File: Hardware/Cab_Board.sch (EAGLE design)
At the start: 154 parts, among them J6 3PCV-03-006, SW1 MF-SW-TACT-4.2MM, SW2 MF-SW-TACT-4.2MM, SW3 MF-SW-TACT-4.2MM, U1 P8X32A-Q44, U10 MAX31855KASA+, U11 MAX31855KASA+, U12 G3VM-61GR2(TR05), U13 G3VM-61GR2(TR05), U14 CD74HC595M96, U15 G3VM-61GR2(TR05), U16 CD74HC165M96, U17 G3VM-61GR2(TR05), U18 G3VM-61GR2(TR05), U19 G3VM-61GR2(TR05), U2 G3VM-61GR2(TR05), U20 G3VM-61GR2(TR05), U21 G3VM-61GR2(TR05), U22 G3VM-61GR2(TR05), U23 G3VM-61GR2(TR05), U24 G3VM-61GR2(TR05), U25 G3VM-61GR2(TR05), U26 G3VM-61GR2(TR05), U27 FXOS8700CQR1, U28 ACPL-C870-000E, U29 MAX11613EUA+, U3 G3VM-61GR2(TR05), U30 TPS7B6933QDCYRQ1, U4 MAX31855KASA+, U5 LM22678TJ-5.0/NOPB, U6 ADP3338AKCZ-3.3-RL, U7 CAT24C512WI-GT3, U8 G3VM-61GR2(TR05), U9 MAX31855KASA+, X1 ABMM-6.000MHZ-B2-T

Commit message: new power input
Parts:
- removed 3.3V, 5V: (no value), PP_Connectors:TEST_POINT_SINGLE_KEYSTONE_5115-5119
- removed 3.3V_PWR: MF-LED-0805-RED, PP_LED:LED_SINGLE_0805
- removed C14: 1uf, PP_Passives:CAPACITOR_NON_POLAR_0805
- removed C15: 1000uF, PP_Passives:CAPACITOR_POLARIZED_10MM_SMD
- removed C16, C23, C32, C33, C34, C35, C38, C39: 0.1uF, PP_Passives:CAPACITOR_NON_POLAR_0805
- removed C17: 10uF, PP_Passives:CAPACITOR_NON_POLAR_1206
- removed C22, C44, C45: 10uF, PP_Passives:CAPACITOR_NON_POLAR_1210
- removed C24: 47uF, PP_Passives:CAPACITOR_POLARIZED_6.3MM_SMD
- removed C27: 0.01uF, PP_Passives:CAPACITOR_NON_POLAR_0805
- removed C28: 180uF, PP_Passives:CAPACITOR_POLARIZED_8MM_SMD
- removed C29, C30: 4.7uF, PP_Passives:CAPACITOR_NON_POLAR_1210
- removed C42: .1uF, PP_Passives:CAPACITOR_NON_POLAR_0603
- removed D10, D7, D8, D9: NUP2105LT1G, PP_Passives:TVS_DIODE_DUALSOT-23
- removed J2, J3, J4, J5: (no value), PP_Connectors:CON_01X02_1546215-2
- removed L3: 6.8uH, PP_Passives:INDUCTOR_IHLP-5050
- removed PROP_TC: TC2030-NL, PP_Connectors:CON_02X03_TC2030
- removed PROP_UART: (no value), PP_Connectors:CON_01X06_2.54MM_PIN_HEADER
- removed R11: 330, PP_Passives:RESISTOR_0603
- removed R2: 470K, PP_Passives:RESISTOR_0603
- removed R28, R29, R30, R31, R32, R33, R34, R35, R36, R37, R38, R39, R40, R41, R42, R43, R44, R45: (no value), MF_Passives:RESISTOR_0603
- removed RELAYS, SWITCHS: (no value), PP_Connectors:CON_01X10_1-282834-0
- removed U10, U11, U4, U9: MAX31855KASA+, PP_Sensors:MAX31855
- removed U12, U13, U15, U17, U18, U19, U20, U21, U22, U23, U24, U25, U26, U8: G3VM-61GR2(TR05), PP_DigitalIC:G3VM-61GR2
- removed U14: CD74HC595M96, PP_DigitalIC:CD74HC595M96
- removed U16: CD74HC165M96, PP_DigitalIC:CD74HC165M96
- removed U28: ACPL-C870-000E, PP_AnalogIC:ACPL-C87X
- removed U30: TPS7B6933QDCYRQ1, MF_IC_Power:TPS7B6933QDCYRQ1
- removed U5: LM22678TJ-5.0/NOPB, PP_PowerIC:LM22678
- removed U6: ADP3338AKCZ-3.3-RL, PP_PowerIC:LINEAR_VOTLAGE_REGULATORS_ADP3338
- added C20: 0.1uF, PP_Passives:CAPACITOR_NON_POLAR_0805
- added D1: TPSMB33A, PP_Passives:DIODE_DO-214AA
- added FTDI_CABLE: (no value), PP_Connectors:CON_01X06_2.54MM_PIN_HEADER
- added L1: XPL2010-104MLC, PP_Passives:INDUCTOR_XPL2010
- added TAG_CONNECT: TC2030-NL, PP_Connectors:CON_02X03_TC2030
- C1, C11, C12, C2, C25, C26, C3, C31, C37, C4, C40, C5, C7, C8: MPN (none) -> MF-CAP-0805-0.1uF
- C10: MPN GRJ32DC72A475KE11L -> UMJ325AB7475KMHP
- C13: value 4.7uF -> 470uF; device PP_Passives:CAPACITOR_NON_POLAR_1210 -> PP_Passives:CAPACITOR_POLARIZED_10MM_SMD; MPN GRJ32DC72A475KE11L -> EEH-ZS1V471P
- C36: device PP_Passives:CAPACITOR_NON_POLAR_0805 -> PP_Passives:CAPACITOR_NON_POLAR_1206; MPN (none) -> GRJ32DC72A475KE11L
- C41, C43: value .1uF -> 0.1uF; device PP_Passives:CAPACITOR_NON_POLAR_0603 -> PP_Passives:CAPACITOR_NON_POLAR_0805; MPN (none) -> MF-CAP-0805-0.1uF
- C6: device PP_Passives:CAPACITOR_NON_POLAR_1210 -> PP_Passives:CAPACITOR_NON_POLAR_1206; MPN (none) -> MF-CAP-1206-10uF
- C9: value 0.1uF -> 1uF; MPN (none) -> C0805X105K5RACAUTO
- D3: value VB20100S-E3/8W -> TPSMB18A; device PP_Passives:DIODE_D2PAK(TO-263AB) -> PP_Passives:DIODE_DO-214AA; MPN (none) -> TPSMB18A
- DISP1: MPN (none) -> 61201621621
- J1: value (none) -> 3PCV-04-006; device PP_Connectors:CON_01X02_1546215-2 -> PP_Connectors:CON_01X04_3PCV-04-006; LABEL01 T+ -> ANALOG 0; LABEL02 T- -> ANALOG 1; LABEL03 (none) -> ANALOG 3; LABEL04 (none) -> ANALOG 4; MPN (none) -> 3PCV-04-006
- R10, R17, R9: device PP_Passives:RESISTOR_0805 -> PP_Passives:RESISTOR_0603; MPN (none) -> MF-RES-0603-10K
- R12, R13: MPN (none) -> MF-RES-0603-10K
- R14, R18, R3, R4, R5, R6, R7, R8: value 120 -> 100; MPN (none) -> MF-RES-0603-100
- R15, R16: value 10K -> 15K; device PP_Passives:RESISTOR_0805 -> PP_Passives:RESISTOR_0603; MPN (none) -> MF-RES-0603-15K
- R19, R20: value (none) -> 15K; device MF_Passives:RESISTOR_0603 -> PP_Passives:RESISTOR_0603; MPN (none) -> MF-RES-0603-15K
- R21, R22, R23, R24: value (none) -> 4.7K; device MF_Passives:RESISTOR_0603 -> PP_Passives:RESISTOR_0603; MPN (none) -> MF-RES-0603-4.7K
- R25, R26, R27: value (none) -> 100; device MF_Passives:RESISTOR_0603 -> PP_Passives:RESISTOR_0603; MPN (none) -> MF-RES-0603-100
- SW_D, SW_S, SW_U: value (none) -> 1546215-2; MPN (none) -> 1546215-2
- U2: value G3VM-61GR2(TR05) -> LT8672EMS#PBF; device PP_DigitalIC:G3VM-61GR2 -> PP_PowerIC:LT8672EMS#PBF; MPN (none) -> LT8672EMS#PBF
- U27: MPN (none) -> FXOS8700CQR1
- U29: MPN (none) -> MAX11613EUA+
- U3: value G3VM-61GR2(TR05) -> IPD100N06S403ATMA2; device PP_DigitalIC:G3VM-61GR2 -> PP_DiscreteSemi:MOSFET_N-CHANNEL_SINGLE_TO-252-3; MPN (none) -> IPD100N06S403ATMA2
- U7: MPN (none) -> CAT24C512WI-GT3
- X1: value ABMM-6.000MHZ-B2-T -> 6.0MHz; device MF_Frequency_Control:XTL_7MMX5MM -> MF_Frequency_Control:CYRSTAL_GND_ABMM; MPN (none) -> ABMM-6.000MHZ-B2-T
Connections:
- removed net 12V_BATT_ON: C44.1, U30.VIN
- removed net 5V_PWR: C6.1, DISP1.VCC
- removed net CHASSIS_GND: C44.2, C45.2, R44.P$1, U12.3, U13.3, U15.3, U17.3, U18.3, U19.CATHODE, U2.3, U20.CATHODE, U21.CATHODE, U22.CATHODE, U23.CATHODE, U24.CATHODE, U25.CATHODE, U26.CATHODE, U28.GND1, U28.SHDN, U3.3, U30.GND/ADJ, U8.3
- removed net EXT_5V: C45.1, U28.VDD1, U30.VOUT
- removed net IN_OPTO_1: R29.P$1, U16.D1, U20.4
- removed net IN_OPTO_2: R30.P$1, U16.D2, U21.4
- removed net IN_OPTO_3: R31.P$1, U16.D3, U22.4
- removed net IN_OPTO_4: R32.P$1, U16.D4, U23.4
- removed net IN_OPTO_5: R33.P$1, U16.D5, U24.4
- removed net IN_OPTO_6: R34.P$1, U16.D6, U25.4
- removed net IN_OPTO_7: R35.P$1, U16.D7, U26.4
- removed net N$16: R24.P$2, U15.ANODE
- removed net N$17: R25.P$2, U17.ANODE
- removed net N$18: R26.P$2, U18.ANODE
- removed net N$19: R39.P$1, U23.ANODE
- removed net N$20: R40.P$1, U24.ANODE
- removed net N$21: R41.P$1, U25.ANODE
- removed net N$22: R42.P$1, U26.ANODE
- removed net N$23: R27.P$2, SWITCHS.1
- removed net N$24: R36.P$2, SWITCHS.2
- removed net N$25: R37.P$2, SWITCHS.3
- removed net N$26: R38.P$2, SWITCHS.4
- removed net N$27: R39.P$2, SWITCHS.5
- removed net N$28: R40.P$2, SWITCHS.6
- removed net N$29: R41.P$2, SWITCHS.7
- removed net N$30: R42.P$2, SWITCHS.8
- removed net N$31: R2.2, U5.EN
- removed net N$32: C42.1, R43.P$1, U28.VOUT+
- removed net N$33: R44.P$2, R45.P$2, U28.VIN
- removed net N$36: J5.PIN1, R45.P$1
- removed net N$5: C27.2, D3.CATHODE, L3.P$2, U5.SW
- removed net OUT_0: R19.P$1, U14.Q0
- removed net OUT_1: R20.P$1, U14.Q1
- removed net OUT_2: R21.P$1, U14.Q2
- removed net OUT_3: R22.P$1, U14.Q3
- removed net OUT_4: R23.P$1, U14.Q4
- removed net OUT_5: R24.P$1, U14.Q5
- removed net OUT_6: R25.P$1, U14.Q6
- removed net OUT_7: R26.P$1, U14.Q7
- removed net RLY_0: RELAYS.1, U2.4
- removed net RLY_1: RELAYS.2, U3.4
- removed net RLY_2: RELAYS.3, U8.4
- removed net RLY_3: RELAYS.4, U12.4
- removed net RLY_4: RELAYS.5, U13.4
- removed net RLY_5: RELAYS.6, U15.4
- removed net RLY_6: RELAYS.7, U17.4
- removed net RLY_7: RELAYS.8, U18.4
- removed net SCL_1: R12.1, U1.P10, U27.SCL/SCKL, U29.SCL
- removed net SDA_1: R13.1, U1.P9, U27.SDA/MOSI, U29.SDA
- removed net T+_0: C33.1, D8.1, J1.PIN1, U9.T+
- removed net T+_1: C35.1, D9.1, J2.PIN1, U10.T+
- removed net T+_2: C39.1, D7.1, J3.PIN1, U11.T+
- removed net T+_3: C12.1, D10.1, J4.PIN1, U4.T+
- removed net T-_0: C33.2, D8.2, J1.PIN2, U9.T-
- removed net T-_1: C35.2, D9.2, J2.PIN2, U10.T-
- removed net T-_2: C39.2, D7.2, J3.PIN2, U11.T-
- removed net T-_3: C12.2, D10.2, J4.PIN2, U4.T-
- new net P10: U1.P10
- new net P9: U1.P9
- new net VIN: D1.CATHODE, U2.SOURCE, U3.SOURCE
- net !RES!_PROP: now also FTDI_CABLE.6, TAG_CONNECT.PIN6; no longer PROP_TC.PIN6, PROP_UART.6
- net 12V: no longer C10.1, C14.1, C29.1, C30.1, R2.1, U5.VIN
- net 165_CLK: no longer U16.CLK
- net 165_DATA: no longer U16.QH
- net 165_LOAD: no longer U16.LAT
- net 3.3V: no longer 3.3V.P$1, C11.1, C22.1, C23.1, C24.POS, C32.1, C34.1, C38.1, C7.1, C9.1, R11.1, R15.2, R16.2, R28.P$2, R29.P$2, R30.P$2, R31.P$2, R32.P$2, R33.P$2, R34.P$2, R35.P$2, U10.VCC, U11.VCC, U14.MR, U14.VCC, U16.VCC, U28.VDD2, U4.VCC, U6.OUT, U9.VCC
- net 595_CLK: no longer U14.SHCP
- net 595_DATA: no longer U14.DS
- net 595_LAT: no longer U14.STCP
- net 5V: now also C6.1, DISP1.VCC; no longer 5V.P$1, C13.1, C15.POS, C16.1, C17.1, C28.POS, L3.P$1, U5.FB, U6.IN
- net A0: now also C7.1, R15.1, R24.2; no longer R43.P$2
- net A1: now also C11.1, R16.1, R23.2
- net A2: now also C12.1, R19.1, R22.2
- net A3: now also C20.1, R20.1, R21.2
- net GND: now also C12.2, C13.NEG, C20.2, D3.CATHODE, FTDI_CABLE.1, R21.1, R22.1, R23.1, R24.1, TAG_CONNECT.PIN5, U2.GND; no longer 3.3V_PWR.CATHODE, C13.2, C14.2, C15.NEG, C16.2, C17.2, C22.2, C23.2, C24.NEG, C28.NEG, C29.2, C30.2, C32.2, C34.2, C38.2, C42.2, C9.2, D10.3, D3.ANODE, D7.3, D8.3, D9.3, PROP_TC.PIN5, PROP_UART.1, U10.GND, U11.GND, U12.CATHODE, U13.CATHODE, U14.GND, U14.OE, U15.CATHODE, U16.C_INH, U16.GND, U17.CATHODE, U18.CATHODE, U19.3, U2.CATHODE, U20.3, U21.3, U22.3, U23.3, U24.3, U25.3, U26.3, U28.GND2, U28.VOUT-, U3.CATHODE, U4.GND, U5.GND, U6.GND, U8.CATHODE, U9.GND
- net N$1: now also J1.1, R15.2; no longer R28.P$1, U16.D0, U19.4
- net N$10: now also R25.2, SW_U.PIN1; no longer R38.P$1, U22.ANODE
- net N$11: now also R26.2, SW_S.PIN1; no longer R19.P$2, U2.ANODE
- net N$12: now also R27.2, SW_D.PIN1; no longer R20.P$2, U3.ANODE
- net N$13: now also C10.1, C13.POS, C9.1, L1.P$1, U2.DRAIN, U3.DRAIN; no longer R21.P$2, U8.ANODE
- net N$14: now also C9.2, U2.AUX; no longer R22.P$2, U12.ANODE
- net N$15: now also L1.P$2, U2.AUXSW; no longer R23.P$2, U13.ANODE
- net N$2: now also U2.GATE, U3.GATE; no longer C27.1, U5.BOOT
- net N$3: now also J1.2, R16.2; no longer R27.P$1, U19.ANODE
- net N$4: now also J1.3, R19.2; no longer R36.P$1, U20.ANODE
- net N$6: now also J1.4, R20.2; no longer R37.P$1, U21.ANODE
- net N$9: now also D1.ANODE, D3.ANODE; no longer 3.3V_PWR.ANODE, R11.2
- net RX_PROP: now also FTDI_CABLE.4, TAG_CONNECT.PIN4; no longer PROP_TC.PIN4, PROP_UART.4
- net SCL: now also R12.1, U27.SCL/SCKL, U29.SCL; no longer R15.1
- net SDA: now also R13.1, U27.SDA/MOSI, U29.SDA; no longer R16.1
- net SW_D: now also R27.1; no longer SW_D.PIN1
- net SW_S: now also R26.1; no longer SW_S.PIN1
- net SW_U: now also R25.1; no longer SW_U.PIN1
- net TC_CS_0: no longer U9.!CS
- net TC_CS_1: no longer U10.!CS
- net TC_CS_2: no longer U11.!CS
- net TC_CS_3: no longer U4.!CS
- net TC_SCK: no longer U10.SCK, U11.SCK, U4.SCK, U9.SCK
- net TC_SO: no longer U10.SO, U11.SO, U4.SO, U9.SO
- net TX_PROP: now also FTDI_CABLE.5, TAG_CONNECT.PIN3; no longer PROP_TC.PIN3, PROP_UART.5
- net X0: now also X1.X1; no longer X1.X0
- net X1: now also X1.X0; no longer X1.X1
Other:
- note added: "ANALOG INPUT 12V COMPLIANT"
- note added: "DISPLAY VFD CONNECTOR"
- note added: "EEPROM FOR PROPELLER"
- note added: "IMU AND GYRO"
- note added: "NAV BUTTONS"
- note added: "PROPELLER MCU"
- note added: "PROPELLER PROGRAMMING SETUP"
- note removed: "5V POWER SUPPLY"
- moved on the sheet: 12V, C1, C10, C11, C12, C18, C19, C2, C25, C26, C3, C31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

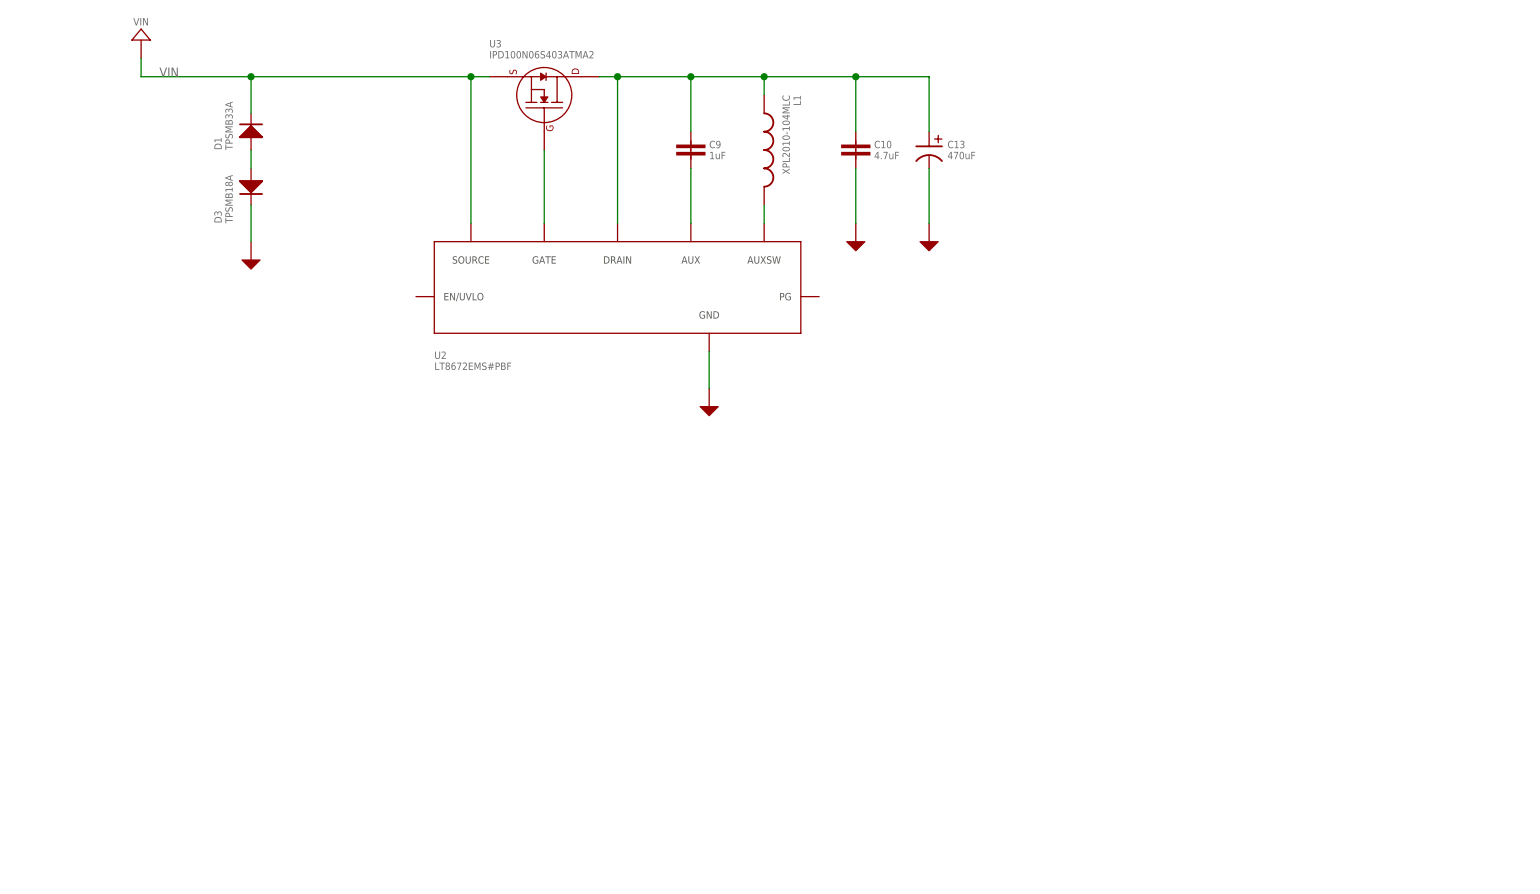
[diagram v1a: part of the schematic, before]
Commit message: added LT8614
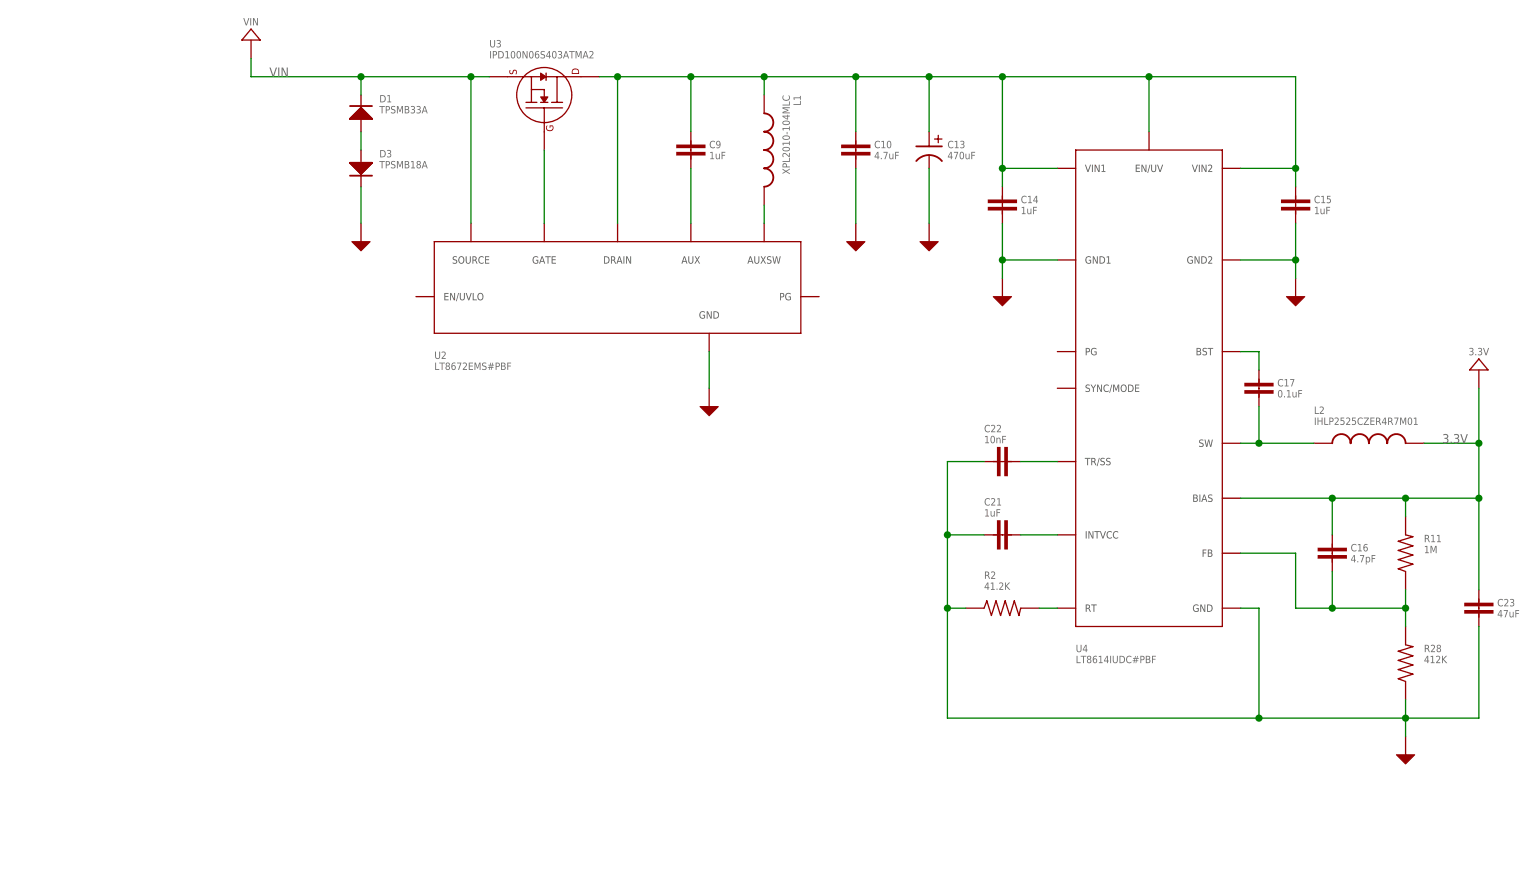
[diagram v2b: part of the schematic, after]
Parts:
- added C14, C15, C21: 1uF, PP_Passives:CAPACITOR_NON_POLAR_0805
- added C16: 4.7pF, PP_Passives:CAPACITOR_NON_POLAR_0603
- added C17: 0.1uF, PP_Passives:CAPACITOR_NON_POLAR_0603
- added C22: 10nF, PP_Passives:CAPACITOR_NON_POLAR_0603
- added C23: 47uF, PP_Passives:CAPACITOR_NON_POLAR_1210
- added L2: IHLP2525CZER4R7M01, PP_Passives:INDUCTOR_IHLP-2525
- added R11: 1M, PP_Passives:RESISTOR_0603
- added R2: 41.2K, PP_Passives:RESISTOR_0603
- added R28: 412K, PP_Passives:RESISTOR_0603
- added U4: LT8614IUDC#PBF, PP_PowerIC:LT8614IUDC#PBF
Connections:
- new net BST: C17.1, U4.BST
- new net FB: C16.2, R11.1, R28.2, U4.FB
- new net INTVCC: C21.2, U4.INTVCC
- new net RT: R2.2, U4.RT
- new net SW: C17.2, L2.P$1, U4.SW
- new net TR/SS: C22.2, U4.TR/SS
- net 3.3V: now also C16.1, C23.1, L2.P$2, R11.2, U4.BIAS
- net GND: now also C14.2, C15.2, C21.1, C22.1, C23.2, R2.1, R28.1, U4.GND, U4.GND1, U4.GND2
- net N$13: now also C14.1, C15.1, U4.EN/UV, U4.VIN1, U4.VIN2
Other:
- moved on the sheet: D1, D3

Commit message: cleaing up schematic more.
8 analog inputs
0-5V Analog in
Thermistors
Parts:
- removed 12V, GND: (no value), PP_Connectors:TEST_POINT_SINGLE_KEYSTONE_5115-5119
- removed C11, C12, C20, C25, C26, C37, C40, C41, C43, C7: 0.1uF, PP_Passives:CAPACITOR_NON_POLAR_0805
- removed C18: 1000uF, PP_Passives:CAPACITOR_POLARIZED_12.5MM_PTH
- removed C19: 220uF, PP_Passives:CAPACITOR_POLARIZED_10MM_SMD
- removed C36: 4.7uF, PP_Passives:CAPACITOR_NON_POLAR_1206
- removed C6: 10uF, PP_Passives:CAPACITOR_NON_POLAR_1206
- removed DISP1: 61201621621, PP_Displays:CU40056-UW1J
- removed J1: 3PCV-04-006, PP_Connectors:CON_01X04_3PCV-04-006
- removed J6: 3PCV-03-006, PP_Connectors:CON_01X03_3PV-03-006
- removed R10, R12, R13, R17, R9: 10K, PP_Passives:RESISTOR_0603
- removed R14, R18, R25, R26, R27, R3, R4, R5, R6, R7, R8: 100, PP_Passives:RESISTOR_0603
- removed R15, R16, R19, R20: 15K, PP_Passives:RESISTOR_0603
- removed R21, R22, R23, R24: 4.7K, PP_Passives:RESISTOR_0603
- removed SW1, SW2, SW3: MF-SW-TACT-4.2MM, MF_Switches:TACT_4.2MM
- removed SW_D, SW_S, SW_U: 1546215-2, PP_Connectors:CON_01X02_1546215-2
- removed TVS1: V18AUMLA2220H, PP_Passives:TVS_DIODE_2220
- removed U27: FXOS8700CQR1, PP_Sensors:FXOS8700CQR1
- removed U29: MAX11613EUA+, PP_AnalogIC:MAX11613EUA+
- added C24, C27, C30: 1uF, PP_Passives:CAPACITOR_NON_POLAR_0805
- added C28: 4.7pF, PP_Passives:CAPACITOR_NON_POLAR_0603
- added C29: 0.1uF, PP_Passives:CAPACITOR_NON_POLAR_0603
- added C32: 10nF, PP_Passives:CAPACITOR_NON_POLAR_0603
- added C33: 47uF, PP_Passives:CAPACITOR_NON_POLAR_1210
- added J2: TBL009-254-02GY-2GY, PP_Connectors:CON_01X02_TBL009-254-02GY-2GY
- added L3: IHLP2525CZER4R7M01, PP_Passives:INDUCTOR_IHLP-2525
- added R29: 41.2K, PP_Passives:RESISTOR_0603
- added R30: 1M, PP_Passives:RESISTOR_0603
- added R31: 243K, PP_Passives:RESISTOR_0603
- added U5: LT8614IUDC#PBF, PP_PowerIC:LT8614IUDC#PBF
- C31: SPICEPREFIX (none) -> C
- D2: value VS-12CWQ10FN-M3 -> BAT54S; device PP_Passives:DIODE_D-PAK(TO-252AA) -> PP_Passives:TVS_DIODE_DUALSOT-23; MPN VS-12CWQ10FN-M3 -> (none)
- U7: SPICEPREFIX (none) -> X
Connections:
- net 165_CLK renamed P13
- net 165_DATA renamed P11
- net 165_LOAD renamed P12
- net 595_CLK renamed P16
- net 595_DATA renamed P14
- net 595_LAT renamed P15
- net TC_CS_0 renamed P22
- net TC_CS_1 renamed P23
- net TC_CS_2 renamed P24
- net TC_CS_3 renamed P25
- net TC_SCK renamed P27
- net TC_SO renamed P26
- removed net 12V: 12V.P$1, C18.POS, C19.POS, D2.CATHODE
- removed net 12V_BATT: D2.ANODE, J6.PIN1, TVS1.P$2
- removed net 5V: C6.1, DISP1.VCC
- removed net A0: C7.1, R15.1, R24.2, U29.A_0
- removed net A1: C11.1, R16.1, R23.2, U29.A_1
- removed net A2: C12.1, R19.1, R22.2, U29.A_2
- removed net A3: C20.1, R20.1, R21.2, U29.A_3
- removed net D4: DISP1.D4, R6.2
- removed net D5: DISP1.D5, R5.2
- removed net D6: DISP1.D6, R4.2
- removed net D7: DISP1.D7, R3.2
- removed net DOME_PWR: J6.PIN3
- removed net E1: DISP1.E1, R8.2
- removed net E2: DISP1.E2, R7.2
- removed net N$1: J1.1, R15.2
- removed net N$10: R25.2, SW_U.PIN1
- removed net N$11: R26.2, SW_S.PIN1
- removed net N$12: R27.2, SW_D.PIN1
- removed net N$3: J1.2, R16.2
- removed net N$4: J1.3, R19.2
- removed net N$6: J1.4, R20.2
- removed net N$7: C26.1, U27.BYP
- removed net N$8: C40.1, U27.CRST
- removed net PROP_D4: R6.1, U1.P3
- removed net PROP_D5: R5.1, U1.P4
- removed net PROP_D6: R4.1, U1.P1
- removed net PROP_D7: R3.1, U1.P2
- removed net PROP_E1: R8.1, U1.P5
- removed net PROP_E2: R7.1, U1.P8
- removed net PROP_R/W: R14.1, U1.P6
- removed net PROP_RS: R18.1, U1.P7
- removed net R/W: DISP1.R/W, R14.2
- removed net RS: DISP1.RS, R18.2
- removed net SW_D: R27.1, R9.2, SW3.P$1, U1.P19
- removed net SW_S: R10.2, R26.1, SW2.P$1, U1.P20
- removed net SW_U: R17.2, R25.1, SW1.P$1, U1.P21
- new net 5.0V: C28.1, C33.1, L3.P$2, R30.2, U5.BIAS
- new net BST1: C29.1, U5.BST
- new net FB1: C28.2, R30.1, R31.2, U5.FB
- new net INTVCC1: C30.2, U5.INTVCC
- new net P1: U1.P1
- new net P19: U1.P19
- new net P2: U1.P2
- new net P20: U1.P20
- new net P21: U1.P21
- new net P3: U1.P3
- new net P4: U1.P4
- new net P5: U1.P5
- new net P6: U1.P6
- new net P7: U1.P7
- new net P8: U1.P8
- new net RT1: R29.2, U5.RT
- new net SW1: C29.2, L3.P$1, U5.SW
- new net TR/SS1: C32.2, U5.TR/SS
- net 3.3V: no longer C25.1, C36.1, C37.1, C41.1, C43.1, R10.1, R12.2, R13.2, R17.1, R9.1, U27.VDD, U27.VDDIO, U29.VCC
- net GND: now also C24.2, C27.2, C30.1, C32.1, C33.2, J2.PIN2, R29.1, R31.1, U5.GND, U5.GND1, U5.GND2; no longer C11.2, C12.2, C18.NEG, C19.NEG, C20.2, C25.2, C26.2, C36.2, C37.2, C40.2, C41.2, C43.2, C6.2, C7.2, DISP1.D0, DISP1.D1, DISP1.D2, DISP1.D3, DISP1.GND, GND.P$1, J6.PIN2, R21.1, R22.1, R23.1, R24.1, SW1.P$4, SW2.P$4, SW3.P$4, SW_D.PIN2, SW_S.PIN2, SW_U.PIN2, TVS1.P$1, U27.GND, U27.RST, U27.SA0/MISO, U27.SA1/CS_B, U29.GND
- net N$13: now also C24.1, C27.1, U5.EN/UV, U5.VIN1, U5.VIN2
- net SCL: no longer R12.1, U27.SCL/SCKL, U29.SCL
- net SDA: no longer R13.1, U27.SDA/MOSI, U29.SDA
- net VIN: now also J2.PIN1
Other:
- note removed: "ANALOG INPUT 12V COMPLIANT"
- note removed: "DISPLAY VFD CONNECTOR"
- note removed: "EEPROM FOR PROPELLER"
- note removed: "IMU AND GYRO"
- note removed: "NAV BUTTONS"
- note removed: "POWER INPUT"
- note removed: "PROPELLER MCU"
- note removed: "PROPELLER PROGRAMMING SETUP"
- moved on the sheet: C1, C2, C3, C31, C4, C5, C8, FTDI_CABLE, R1, TAG_CONNECT, U1, U7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

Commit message: added LTC2986HLX#PBF
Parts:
- added D10, D4, D5, D6, D7, D8, D9: BAT54S, PP_Passives:TVS_DIODE_DUALSOT-23
- added J1: DF11G-16DP-2V(50), PP_Connectors:CON_02X08_DF11G-16DP-2V(50)
- added R10, R3, R4, R5, R6, R7, R8, R9: 330, PP_Passives:RESISTOR_0805
- added U$45: LTC2986HLX#PBF, PP_Sensors:LTC2986HLX#PBF
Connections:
- removed net P0: U1.P0
- removed net P1: U1.P1
- new net ANALOG_MCU_0: D2.3, R3.1
- new net ANALOG_MCU_1: D4.3, R4.1
- new net ANALOG_MCU_2: D5.3, R5.1
- new net ANALOG_MCU_3: D6.3, R6.1
- new net ANALOG_MCU_4: D7.3, R7.1
- new net ANALOG_MCU_5: D8.3, R8.1
- new net ANALOG_MCU_6: D9.3, R9.1
- new net ANALOG_MCU_7: D10.3, R10.1
- new net ANALOG_WORLD_0: R3.2
- new net ANALOG_WORLD_1: R4.2
- new net ANALOG_WORLD_2: R5.2
- new net ANALOG_WORLD_3: R6.2
- new net ANALOG_WORLD_4: R7.2
- new net ANALOG_WORLD_5: R8.2
- new net ANALOG_WORLD_6: R9.2
- new net ANALOG_WORLD_7: R10.2
- new net GPIO0: J1.11
- new net GPIO1: J1.12
- new net GPIO2: J1.9
- new net GPIO3: J1.10
- new net GPIO4: J1.13
- new net LCD_RX: J1.1, U1.P1
- new net LCD_TX: J1.2, U1.P0
- net 5.0V: now also D10.1, D2.1, D4.1, D5.1, D6.1, D7.1, D8.1, D9.1, J1.16
- net GND: now also D10.2, D2.2, D4.2, D5.2, D6.2, D7.2, D8.2, D9.2, J1.15
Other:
- moved on the sheet: D2

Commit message: Control side of LTC2986HLX done.
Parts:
- removed D10, D2, D4, D5, D6, D7, D8, D9: BAT54S, PP_Passives:TVS_DIODE_DUALSOT-23
- removed R10, R6, R7, R8, R9: 330, PP_Passives:RESISTOR_0805
- removed U$45: LTC2986HLX#PBF, PP_Sensors:LTC2986HLX#PBF
- added C11, C12, C18, C19, C35, C36, C6, C7: 0.1uF, PP_Passives:CAPACITOR_NON_POLAR_0805
- added C20: 1uF, PP_Passives:CAPACITOR_NON_POLAR_0805
- added C25, C26, C34: 10uF, PP_Passives:CAPACITOR_NON_POLAR_1210
- added U6: IPD100N06S403ATMA2, PP_DiscreteSemi:MOSFET_N-CHANNEL_SINGLE_TO-252-3
- added U8: TXB0104DR, PP_DigitalIC:TXB0104DR
- R3, R4: value 330 -> 10K; device PP_Passives:RESISTOR_0805 -> PP_Passives:RESISTOR_0603; MPN (none) -> MF-RES-0603-10K
- R5: value 330 -> 18K; device PP_Passives:RESISTOR_0805 -> PP_Passives:RESISTOR_0603
- U2: value LT8672EMS#PBF -> CAT24C512WI-GT3; device PP_PowerIC:LT8672EMS#PBF -> PP_DigitalIC:EEPROM_I2CSOIC-8_W; MPN LT8672EMS#PBF -> CAT24C512WI-GT3; SPICEPREFIX (none) -> X
- U3: value IPD100N06S403ATMA2 -> LT8672EMS#PBF; device PP_DiscreteSemi:MOSFET_N-CHANNEL_SINGLE_TO-252-3 -> PP_PowerIC:LT8672EMS#PBF; MPN IPD100N06S403ATMA2 -> LT8672EMS#PBF
- U7: value CAT24C512WI-GT3 -> LTC2986HLX-1#PBF; device PP_DigitalIC:EEPROM_I2CSOIC-8_W -> PP_Sensors:LTC2986HLX#PBF; MPN CAT24C512WI-GT3 -> LTC2986HLX-1#PBF; SPICEPREFIX X -> (none)
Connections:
- removed net ANALOG_MCU_0: D2.3, R3.1
- removed net ANALOG_MCU_1: D4.3, R4.1
- removed net ANALOG_MCU_2: D5.3, R5.1
- removed net ANALOG_MCU_3: D6.3, R6.1
- removed net ANALOG_MCU_4: D7.3, R7.1
- removed net ANALOG_MCU_5: D8.3, R8.1
- removed net ANALOG_MCU_6: D9.3, R9.1
- removed net ANALOG_MCU_7: D10.3, R10.1
- removed net ANALOG_WORLD_0: R3.2
- removed net ANALOG_WORLD_1: R4.2
- removed net ANALOG_WORLD_2: R5.2
- removed net ANALOG_WORLD_3: R6.2
- removed net ANALOG_WORLD_4: R7.2
- removed net ANALOG_WORLD_5: R8.2
- removed net ANALOG_WORLD_6: R9.2
- removed net ANALOG_WORLD_7: R10.2
- removed net P10: U1.P10
- removed net P11: U1.P11
- removed net P12: U1.P12
- removed net P7: U1.P7
- removed net P8: U1.P8
- removed net P9: U1.P9
- new net 3.3V_!CS: U1.P7, U8.A1
- new net 3.3V_SCK: U1.P10, U8.A4
- new net 3.3V_SDI: U1.P8, U8.A2
- new net 3.3V_SDO: U1.P9, U8.A3
- new net 5V_!CS: U7.!CS, U8.B1
- new net 5V_SCK: U7.SCK, U8.B4
- new net 5V_SDI: U7.SDI, U8.B2
- new net 5V_SDO: U7.SDO, U8.B3
- new net LTC2986_INTERRUPT: R4.1, R5.2, U1.P12
- new net N$1: C19.1, U7.VREF_BYP
- new net N$12: R4.2, U7.INTERRUPT
- new net N$3: C20.1, U7.VREFOUT, U7.VREFP
- new net N$4: C26.1, U7.Q3
- new net N$6: C25.2, U7.Q2
- new net N$7: C25.1, U7.Q1
- new net N$8: C34.1, U7.LDO
- new net SPI_LEVEL_SHIFTER_OE: R3.2, U1.P11, U8.OE
- net 3.3V: now also C36.1, U2.VCC, U8.VCCA; no longer U7.VCC
- net 5.0V: now also C11.1, C12.1, C18.1, C35.1, C6.1, C7.1, U7.!RESET, U7.VDD, U8.VCCB; no longer D10.1, D2.1, D4.1, D5.1, D6.1, D7.1, D8.1, D9.1
- net GND: now also C11.2, C12.2, C18.2, C19.2, C20.2, C26.2, C34.2, C35.2, C36.2, C6.2, C7.2, R3.1, R5.1, U2.A1, U2.A2, U2.WP, U3.GND, U8.GND; no longer D10.2, D2.2, D4.2, D5.2, D6.2, D7.2, D8.2, D9.2, U7.A1, U7.A2, U7.WP
- net N$13: now also U6.DRAIN; no longer U2.DRAIN
- net N$14: now also U3.AUX; no longer U2.AUX
- net N$15: now also U3.AUXSW; no longer U2.AUXSW
- net N$2: now also U6.GATE; no longer U2.GATE
- net SCL: now also U2.SCL; no longer U7.SCL
- net SDA: now also U2.SDA; no longer U7.SDA
- net VIN: now also U6.SOURCE; no longer U2.SOURCE
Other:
- moved on the sheet: C31, C5, FTDI_CABLE, R1, R3, R4, R5, TAG_CONNECT, U2
